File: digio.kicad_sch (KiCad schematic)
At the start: 42 parts, among them J23 Conn_01x04, J24 Conn_01x04, J25 Conn_02x08_Odd_Even, J26 Conn_02x08_Odd_Even, J27 Conn_02x08_Odd_Even, J28 Conn_02x08_Odd_Even, U18 TCA9535PWR(UMW), U19 TCA9535PWR(UMW)

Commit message: WIP v0.2.0 changes
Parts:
- removed J23, J24: Conn_01x04, HL_Connector_Pad_2.54mm:Pad_1x04_P2.54_1.7x1.7_Rect-Oct, symbol Connector_Generic:Conn_01x04
- removed J25, J26, J27, J28: Conn_02x08_Odd_Even, HL_Connector_Pad_2.54mm:Pad_2x08_P2.54_1.7x1.7_Rect-Oct, symbol Connector_Generic:Conn_02x08_Odd_Even
- added J102, J103, J104, J105: Conn_01x08, HL_Connector_Pad_2.54mm:Pad_1x08_P2.54_1.7x1.7_Oct, symbol Connector_Generic:Conn_01x08
- added J42, J44: Conn_01x04, HL_Connector_Pad_2.54mm:Pad_1x04_P2.54_1.7x1.7_Rect, symbol Connector_Generic:Conn_01x04
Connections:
- net SCL2 is gone; now on net SCL: U19.22 (SCL)
- net SDA2 is gone; now on net SDA: U19.23 (SDA)
- net GND: now also J42.1 (Pin_1), J42.2 (Pin_2), J42.3 (Pin_3), J42.4 (Pin_4), J44.1 (Pin_1), J44.2 (Pin_2), J44.3 (Pin_3), J44.4 (Pin_4)
- net P1r00: now also J104.1 (Pin_1)
- net P1r01: now also J104.2 (Pin_2)
- net P1r02: now also J104.3 (Pin_3)
- net P1r03: now also J104.4 (Pin_4)
- net P1r04: now also J104.5 (Pin_5)
- net P1r05: now also J104.6 (Pin_6)
- net P1r06: now also J104.7 (Pin_7)
- net P1r07: now also J104.8 (Pin_8)
- net P1r10: now also J105.8 (Pin_8)
- net P1r11: now also J105.7 (Pin_7)
- net P1r12: now also J105.6 (Pin_6)
- net P1r13: now also J105.5 (Pin_5)
- net P1r14: now also J105.4 (Pin_4)
- net P1r15: now also J105.3 (Pin_3)
- net P1r16: now also J105.2 (Pin_2)
- net P1r17: now also J105.1 (Pin_1)
- net P2r00: now also J102.1 (Pin_1)
- net P2r01: now also J102.2 (Pin_2)
- net P2r02: now also J102.3 (Pin_3)
- net P2r03: now also J102.4 (Pin_4)
- net P2r04: now also J102.5 (Pin_5)
- net P2r05: now also J102.6 (Pin_6)
- net P2r06: now also J102.7 (Pin_7)
- net P2r07: now also J102.8 (Pin_8)
- net P2r10: now also J103.8 (Pin_8)
- net P2r11: now also J103.7 (Pin_7)
- net P2r12: now also J103.6 (Pin_6)
- net P2r13: now also J103.5 (Pin_5)
- net P2r14: now also J103.4 (Pin_4)
- net P2r15: now also J103.3 (Pin_3)
- net P2r16: now also J103.2 (Pin_2)
- net P2r17: now also J103.1 (Pin_1)
- net SCL1 renamed SCL
- net SDA1 renamed SDA

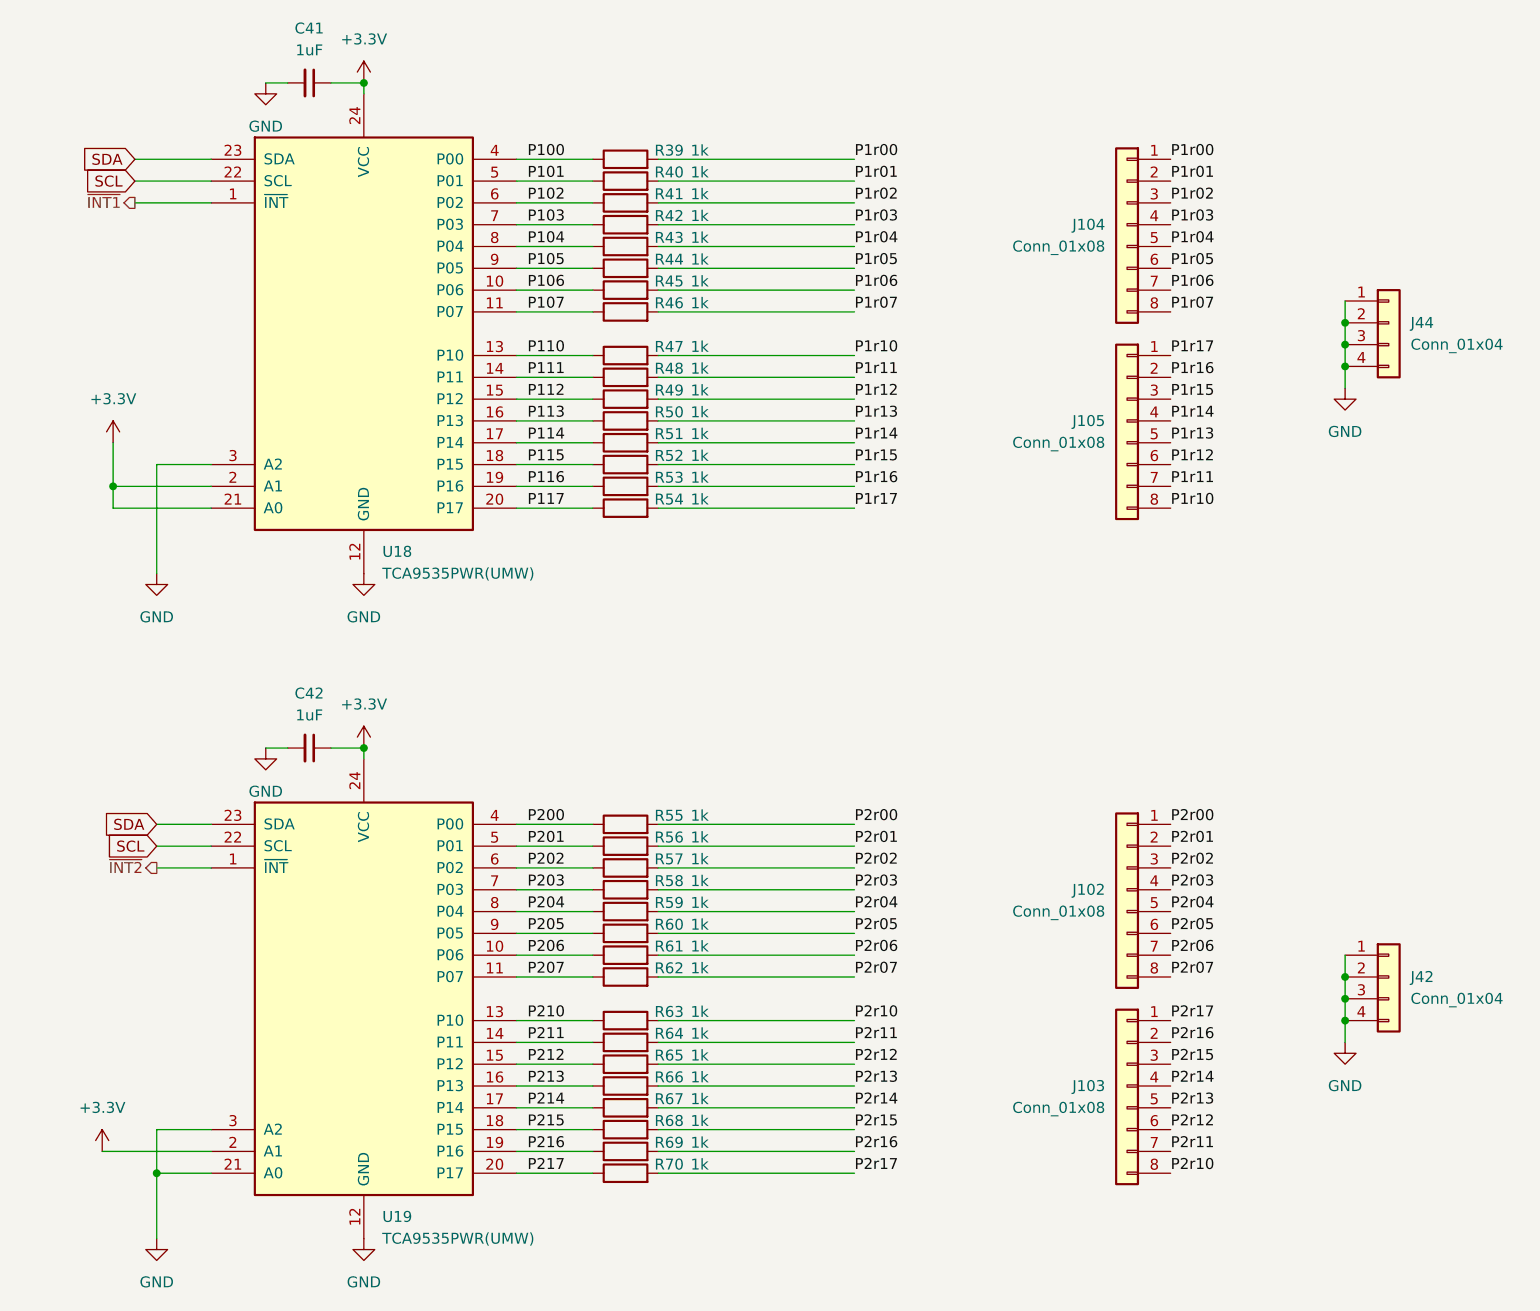
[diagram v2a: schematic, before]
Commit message: Assign part numbers and finish other 0.2.0 changes
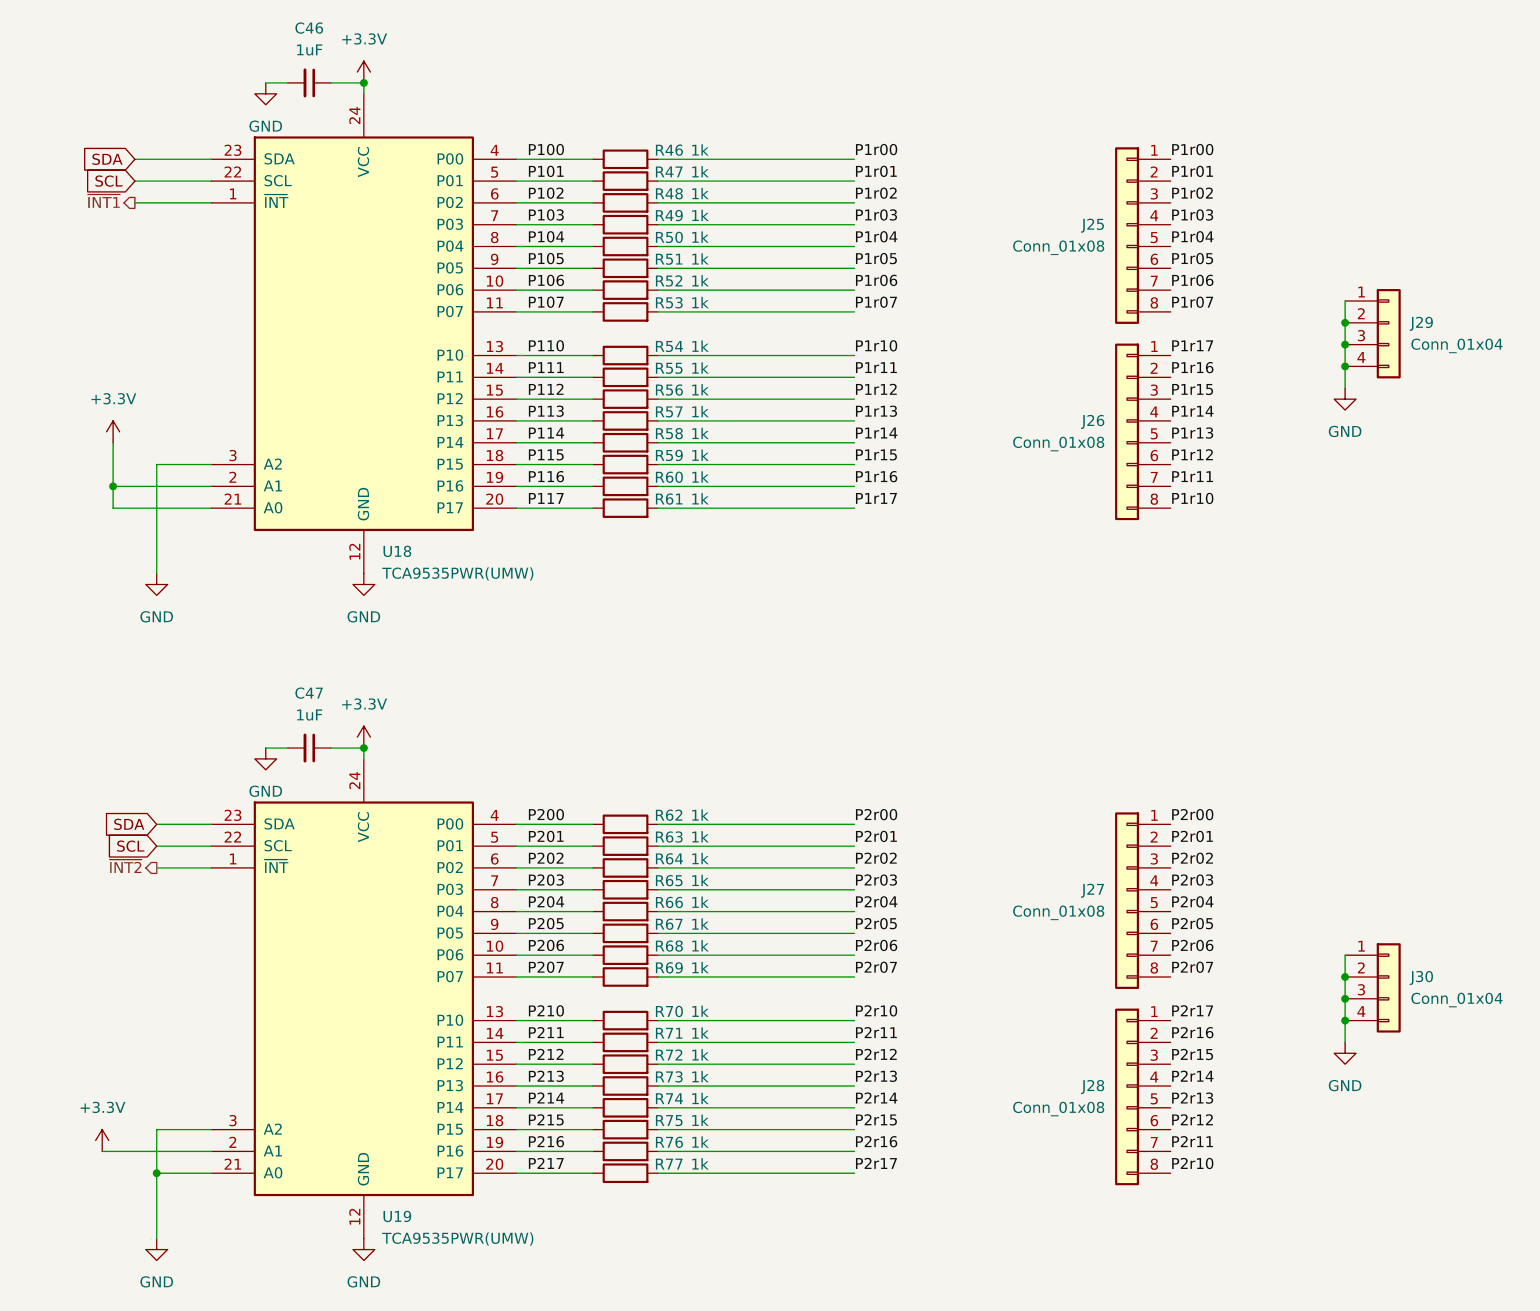
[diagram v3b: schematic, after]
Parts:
- J25: renamed from J104; LCSC (none) -> C492407
- J26: renamed from J105; LCSC (none) -> C492407
- J27: renamed from J102; LCSC (none) -> C492407
- J28: renamed from J103; LCSC (none) -> C492407
- J29: renamed from J44; LCSC (none) -> C2691448
- J30: renamed from J42; LCSC (none) -> C2691448
- renumbered C41 to C46, C42 to C47, R39 to R46, R40 to R47, R41 to R48, R42 to R49, R43 to R50, R44 to R51, R45 to R52, R46 to R53, R47 to R54, R48 to R55, R49 to R56, R50 to R57, R51 to R58, R52 to R59, R53 to R60, R54 to R61, R55 to R62, R56 to R63, R57 to R64, R58 to R65, R59 to R66, R60 to R67, R61 to R68, R62 to R69, R63 to R70, R64 to R71, R65 to R72, R66 to R73, R67 to R74, R68 to R75, R69 to R76, R70 to R77

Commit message: Update the title blocks
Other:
- company: (none) -> Hat Labs Oy
- title: (none) -> HALSPA - Hat Labs Spaghetti Board
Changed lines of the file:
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@@
 	(generator_version "9.0")
 	(paper "A4")
+	(title_block
+		(title "HALSPA - Hat Labs Spaghetti Board")
+		(date "2025-04-17")
+		(rev "v0.2.0")
+		(company "Hat Labs Oy")
+		(comment 1 "See the accompanying LICENSE.md file for license details.")
+	)
 	(junction
 		(at 205.74 53.34)

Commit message: Add JLCPCB corrections
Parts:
- J25, J26, J27, J28: JLCPCB_CORRECTION (none) -> 0;8.89;270
- J29, J30: JLCPCB_CORRECTION (none) -> 0;3.81;270
- U18, U19: LCSC C22396388 -> C130204
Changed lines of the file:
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@@
+			)
+		)
+		(property "JLCPCB_CORRECTION" "0;3.81;270"
+			(at 210.82 53.34 0)
+			(effects
+				(font
+					(size 1.27 1.27)
+				)
+				(hide yes)
 			)
 		)
@@
 			)
 		)
+		(property "JLCPCB_CORRECTION" "0;8.89;270"
+			(at 180.34 142.24 0)
+			(effects
+				(font
+					(size 1.27 1.27)
+				)
+				(hide yes)
+			)
+		)
 		(pin "1"
 		)
@@
 			)
 		)
+		(property "JLCPCB_CORRECTION" "0;8.89;270"
+			(at 180.34 119.38 0)
+			(effects
+				(font
+					(size 1.27 1.27)
+				)
+				(hide yes)
+			)
+		)
 		(pin "1"
 		)
@@
 			)
 		)
-		(property "Datasheet" "https://www.lcsc.com/datasheet/lcsc_datasheet_2410010333_UMW-Youtai-Semiconductor-Co---Ltd--TCA9535PWR-UMW_C22396388.pdf"
+		(property "Datasheet" "https://www.ti.com/lit/ds/symlink/tca9535.pdf"
 			(at 78.74 109.22 0)
 			(effects
@@
 			)
 		)
-		(property "LCSC" "C22396388"
+		(property "LCSC" "C130204"
 			(at 93.5833 162.56 0)
 			(effects
@@
 			)
 		)
-		(property "Datasheet" "https://www.lcsc.com/datasheet/lcsc_datasheet_2410010333_UMW-Youtai-Semiconductor-Co---Ltd--TCA9535PWR-UMW_C22396388.pdf"
+		(property "Datasheet" "https://www.ti.com/lit/ds/symlink/tca9535.pdf"
 			(at 78.74 31.75 0)
 			(effects
@@
 			)
 		)
-		(property "LCSC" "C22396388"
+		(property "LCSC" "C130204"
 			(at 91.44 54.61 0)
 			(effects
@@
 			)
 		)
+		(property "JLCPCB_CORRECTION" "0;8.89;270"
+			(at 180.34 64.77 0)
+			(effects
+				(font
+					(size 1.27 1.27)
+				)
+				(hide yes)
+			)
+		)
 		(pin "1"
 		)
@@
 			)
 		)
+		(property "JLCPCB_CORRECTION" "0;3.81;270"
+			(at 210.82 129.54 0)
+			(effects
+				(font
+					(size 1.27 1.27)
+				)
+				(hide yes)
+			)
+		)
 		(pin "4"
 		)
@@
 			(at 180.34 41.91 0)
 			(effects
+				(font
+					(size 1.27 1.27)
+				)
+				(hide yes)
+			)
+		)
+		(property "JLCPCB_CORRECTION" "0;8.89;270"
+			(at 180.34 41.91 0)
+			(effects

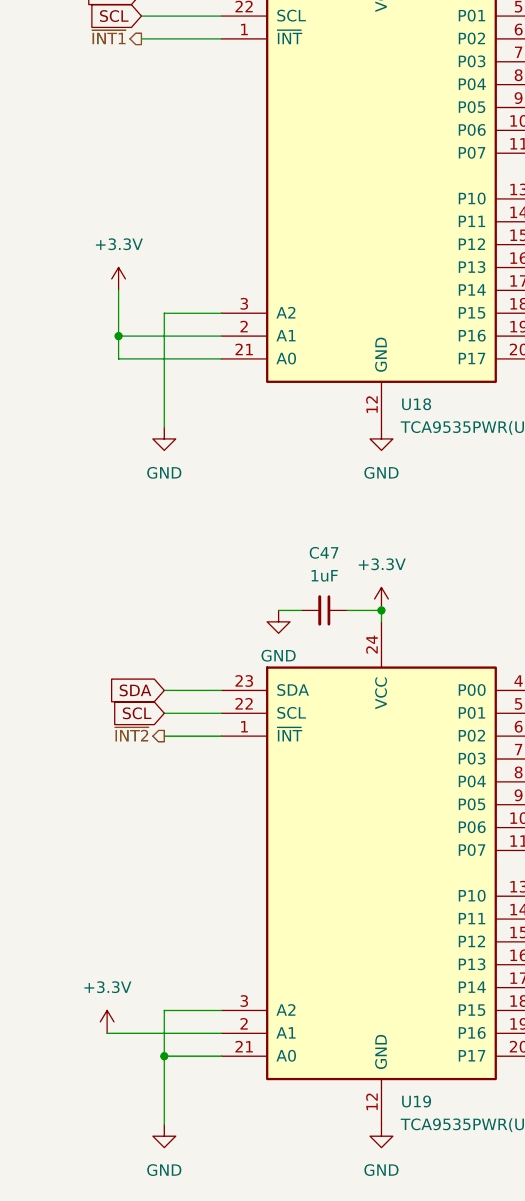
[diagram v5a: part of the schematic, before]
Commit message: Improve schematics labeling
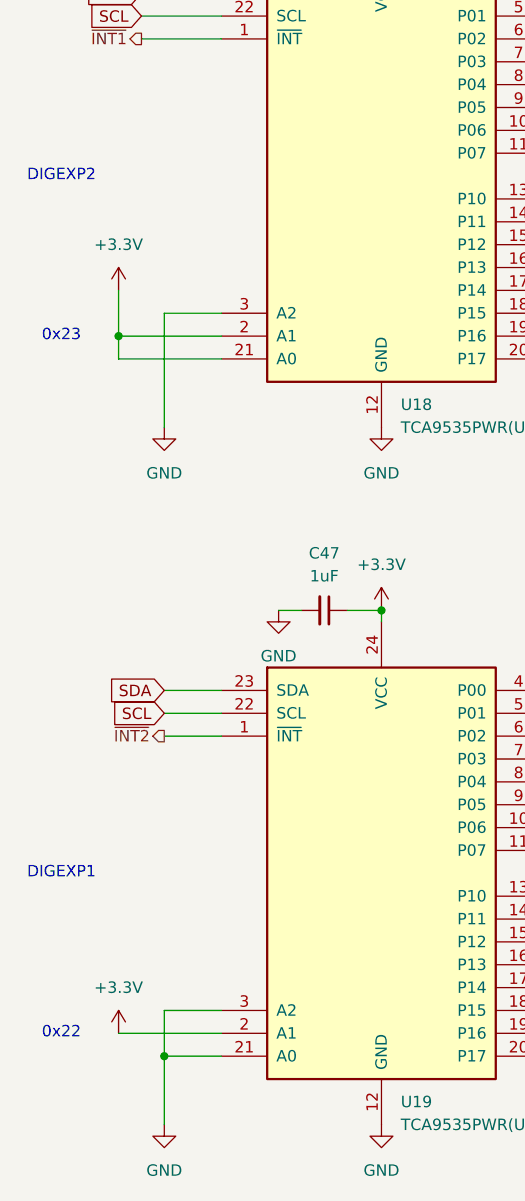
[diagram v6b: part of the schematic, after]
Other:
- note added: "0x22"
- note added: "0x23"
- note added: "DIGEXP1"
- note added: "DIGEXP2"
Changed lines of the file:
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@@
 		(comment 1 "See the accompanying LICENSE.md file for license details.")
 	)
+	(text "0x22"
+		(exclude_from_sim no)
+		(at 55.88 149.86 0)
+		(effects
+			(font
+				(size 1.27 1.27)
+			)
+		)
+	)
+	(text "DIGEXP2"
+		(exclude_from_sim no)
+		(at 55.88 54.61 0)
+		(effects
+			(font
+				(size 1.27 1.27)
+			)
+		)
+	)
+	(text "DIGEXP1"
+		(exclude_from_sim no)
+		(at 55.88 132.08 0)
+		(effects
+			(font
+				(size 1.27 1.27)
+			)
+		)
+	)
+	(text "0x23"
+		(exclude_from_sim no)
+		(at 55.88 72.39 0)
+		(effects
+			(font
+				(size 1.27 1.27)
+			)
+		)
+	)
 	(junction
 		(at 205.74 53.34)
@@
 	(wire
 		(pts
-			(xy 60.96 149.86) (xy 73.66 149.86)
+			(xy 62.23 149.86) (xy 73.66 149.86)
 		)
 		(stroke
@@
 	(symbol
 		(lib_id "power:+3.3V")
-		(at 60.96 149.86 0)
+		(at 62.23 149.86 0)
 		(unit 1)
 		(exclude_from_sim no)
@@
 		(fields_autoplaced yes)
 		(property "Reference" "#PWR0152"
-			(at 60.96 153.67 0)
+			(at 62.23 153.67 0)
 			(effects
 				(font
@@
 		)
 		(property "Value" "+3.3V"
-			(at 60.96 144.78 0)
+			(at 62.23 144.78 0)
 			(effects
 				(font
@@
 		)
 		(property "Footprint" ""
-			(at 60.96 149.86 0)
+			(at 62.23 149.86 0)
 			(effects
 				(font
@@
 		)
 		(property "Datasheet" ""
-			(at 60.96 149.86 0)
+			(at 62.23 149.86 0)
 			(effects
 				(font
@@
 		)
 		(property "Description" "Power symbol creates a global label with name \"+3.3V\""
-			(at 60.96 149.86 0)
+			(at 62.23 149.86 0)
 			(effects
 				(font
